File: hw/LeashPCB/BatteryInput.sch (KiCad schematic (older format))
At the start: 14 parts, among them J201 1020-1, J202 1076-1, J203 1076-1, Q201 CSD18501Q5A, Q202 Q_PMOS_DGS, U201 LM74610Q

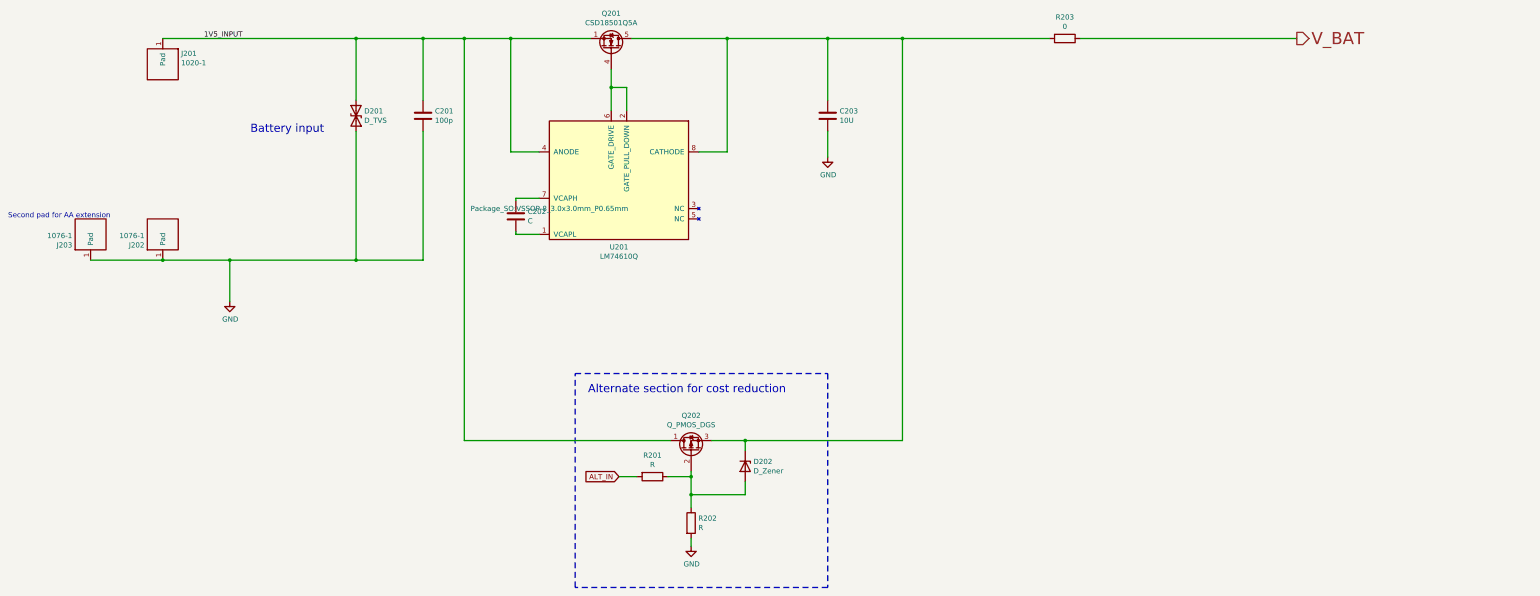
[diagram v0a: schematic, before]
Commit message: Added antenna and routed ideal diode circuit
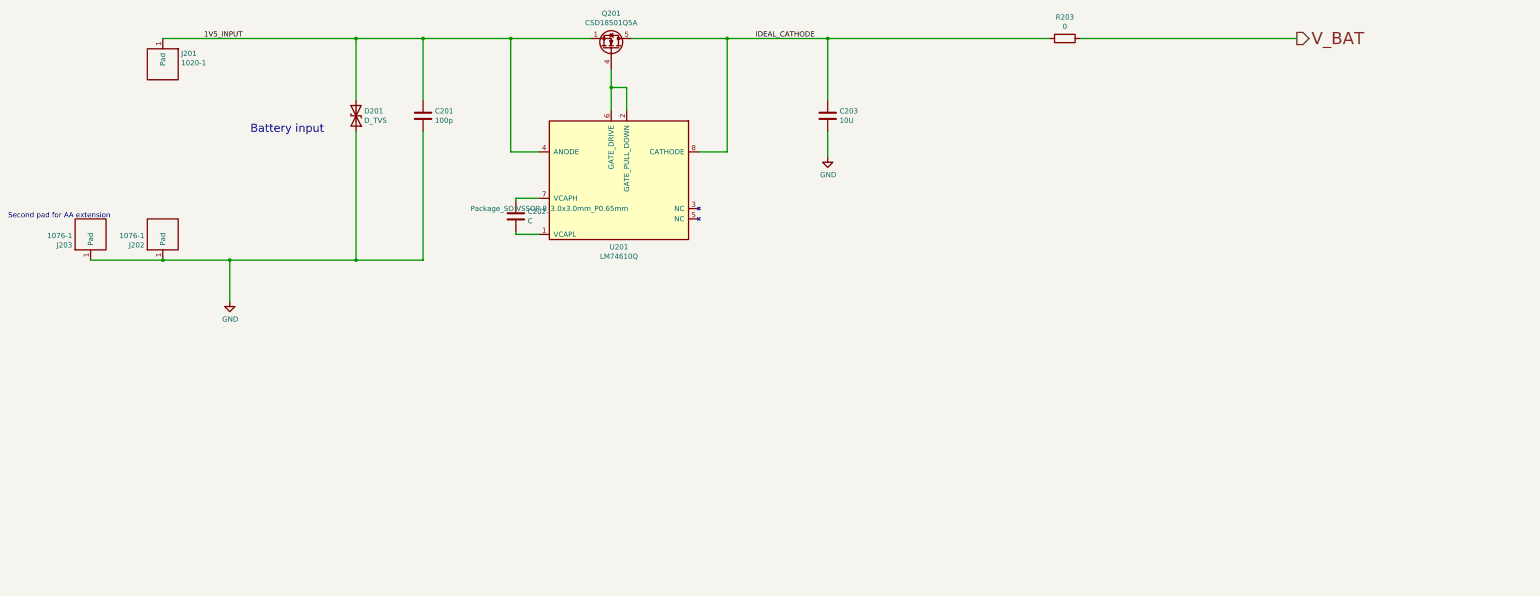
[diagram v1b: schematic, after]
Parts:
- removed D202: D_Zener, symbol Device:D_Zener
- removed Q202: Q_PMOS_DGS, symbol Device:Q_PMOS_DGS
- removed R201, R202: R, Resistor_SMD:R_0402_1005Metric, symbol Device:R
- C203: footprint Capacitor_SMD:C_0402_1005Metric -> Capacitor_SMD:C_0603_1608Metric
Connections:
- net IDEAL_CATHODE: now reaches C203.1, Q201.5 (D), R203.2, U201.8 (CATHODE)
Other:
- note removed: "Alternate section for cost reduction"
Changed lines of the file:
@@
 EESchema Schematic File Version 4
-LIBS:LeashPCB-cache
 EELAYER 29 0
 EELAYER END
@@
 F 0 "C203" H 9065 1621 50  0000 L CNN
 F 1 "10U" H 9065 1530 50  0000 L CNN
-F 2 "Capacitor_SMD:C_0402_1005Metric" H 8988 1425 50  0001 C CNN
+F 2 "Capacitor_SMD:C_0603_1608Metric" H 8988 1425 50  0001 C CNN
 F 3 "~" H 8950 1575 50  0001 C CNN
 	1    8950 1575
@@
 Connection ~ 8950 825
 Wire Wire Line
-	8950 825  9675 825
-Wire Wire Line
 	8950 1725 8950 1975
 Wire Wire Line
@@
 	5875 1925 5875 825
 Connection ~ 5875 825
-Wire Wire Line
-	5875 825  5425 825
 Text Notes 3350 1750 0    79   ~ 0
 Battery input
-Wire Wire Line
-	5425 825  5425 4725
-Connection ~ 5425 825
-Wire Wire Line
-	5425 825  5025 825
-$Comp
-L Device:Q_PMOS_DGS Q202
-U 1 1 5D1B2FC4
-P 7625 4825
-F 0 "Q202" V 7968 4825 50  0000 C CNN
-F 1 "Q_PMOS_DGS" V 7877 4825 50  0000 C CNN
-F 2 "" H 7825 4925 50  0001 C CNN
-F 3 "~" H 7625 4825 50  0001 C CNN
-	1    7625 4825
-	0    -1   -1   0
-$EndComp
-$Comp
-L Device:D_Zener D202
-U 1 1 5D1B5E6D
-P 8150 4975
-F 0 "D202" V 8104 5054 50  0000 L CNN
-F 1 "D_Zener" V 8195 5054 50  0000 L CNN
-F 2 "" H 8150 4975 50  0001 C CNN
-F 3 "~" H 8150 4975 50  0001 C CNN
-	1    8150 4975
-	0    1    1    0
-$EndComp
-$Comp
-L Device:R R202
-U 1 1 5D1B63DF
-P 7625 5525
-F 0 "R202" H 7695 5571 50  0000 L CNN
-F 1 "R" H 7695 5480 50  0000 L CNN
-F 2 "Resistor_SMD:R_0402_1005Metric" V 7555 5525 50  0001 C CNN
-F 3 "~" H 7625 5525 50  0001 C CNN
-	1    7625 5525
-	1    0    0    -1
-$EndComp
-Wire Wire Line
-	5425 4725 7425 4725
-Wire Wire Line
-	7825 4725 8150 4725
-Wire Wire Line
-	8150 4725 8150 4825
-Connection ~ 8150 4725
-Wire Wire Line
-	7625 5025 7625 5075
-Wire Wire Line
-	7625 5675 7625 5750
-Wire Wire Line
-	8150 5125 8150 5250
-Wire Wire Line
-	8150 5250 7625 5250
-Connection ~ 7625 5250
-Wire Wire Line
-	7625 5250 7625 5375
-$Comp
-L power:GND #PWR0103
-U 1 1 5D1BC7E6
-P 7625 5750
-F 0 "#PWR0103" H 7625 5500 50  0001 C CNN
-F 1 "GND" H 7630 5577 50  0000 C CNN
-F 2 "" H 7625 5750 50  0001 C CNN
-F 3 "" H 7625 5750 50  0001 C CNN
-	1    7625 5750
-	1    0    0    -1
-$EndComp
-$Comp
-L Device:R R201
-U 1 1 5D1BDEB4
-P 7250 5075
-F 0 "R201" V 7043 5075 50  0000 C CNN
-F 1 "R" V 7134 5075 50  0000 C CNN
-F 2 "Resistor_SMD:R_0402_1005Metric" V 7180 5075 50  0001 C CNN
-F 3 "~" H 7250 5075 50  0001 C CNN
-	1    7250 5075
-	0    1    1    0
-$EndComp
-Wire Wire Line
-	7400 5075 7625 5075
-Connection ~ 7625 5075
-Wire Wire Line
-	7625 5075 7625 5250
-Wire Wire Line
-	7100 5075 6925 5075
-Text GLabel 6925 5075 0    50   Input ~ 0
-ALT_IN
-Wire Wire Line
-	9675 4725 9675 825
-Wire Wire Line
-	8150 4725 9675 4725
-Connection ~ 9675 825
-Wire Notes Line
-	6500 4075 8950 4075
-Wire Notes Line
-	8950 4075 8950 6150
-Wire Notes Line
-	8950 6150 6500 6150
-Wire Notes Line
-	6500 6150 6500 4075
-Text Notes 6625 4275 0    79   ~ 0
-Alternate section for cost reduction
 $Comp
 L Device:R R203
@@
 	0    1    1    0
 $EndComp
-Wire Wire Line
-	9675 825  11100 825
 Wire Wire Line
 	11400 825  13500 825
@@
 	1800 2975 2500 2975
 Connection ~ 2500 2975
+Text Label 8250 825  0    50   ~ 0
+IDEAL_CATHODE
+Wire Wire Line
+	5025 825  5875 825
+Wire Wire Line
+	8950 825  11100 825
 $EndSCHEMATC

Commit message: Added SWD connector on the back side as a backup for testing and continued routing
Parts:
- J202, J203: footprint leash:1020-1 -> leash:1076-1
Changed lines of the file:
@@
 F 0 "J202" V 2446 2953 50  0000 L CNN
 F 1 "1076-1" V 2537 2953 50  0000 L CNN
-F 2 "leash:1020-1" H 2500 2775 50  0001 C CNN
+F 2 "leash:1076-1" H 2500 2775 50  0001 C CNN
 F 3 "" H 2500 2775 50  0001 C CNN
 F 4 "0.05" H 2500 2775 50  0001 C CNN "Standard Price"
@@
 F 0 "J203" V 1746 2953 50  0000 L CNN
 F 1 "1076-1" V 1837 2953 50  0000 L CNN
-F 2 "leash:1020-1" H 1800 2775 50  0001 C CNN
+F 2 "leash:1076-1" H 1800 2775 50  0001 C CNN
 F 3 "" H 1800 2775 50  0001 C CNN
 F 4 "0.05" H 1800 2775 50  0001 C CNN "Standard Price"

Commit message: Pulled in final small components and finished routing all but the RF section
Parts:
- D201: footprint (none) -> Diode_SMD:D_0402_1005Metric
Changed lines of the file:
@@
 F 0 "D201" V 4329 1654 50  0000 L CNN
 F 1 "D_TVS" V 4420 1654 50  0000 L CNN
-F 2 "" H 4375 1575 50  0001 C CNN
+F 2 "Diode_SMD:D_0402_1005Metric" H 4375 1575 50  0001 C CNN
 F 3 "~" H 4375 1575 50  0001 C CNN
 	1    4375 1575

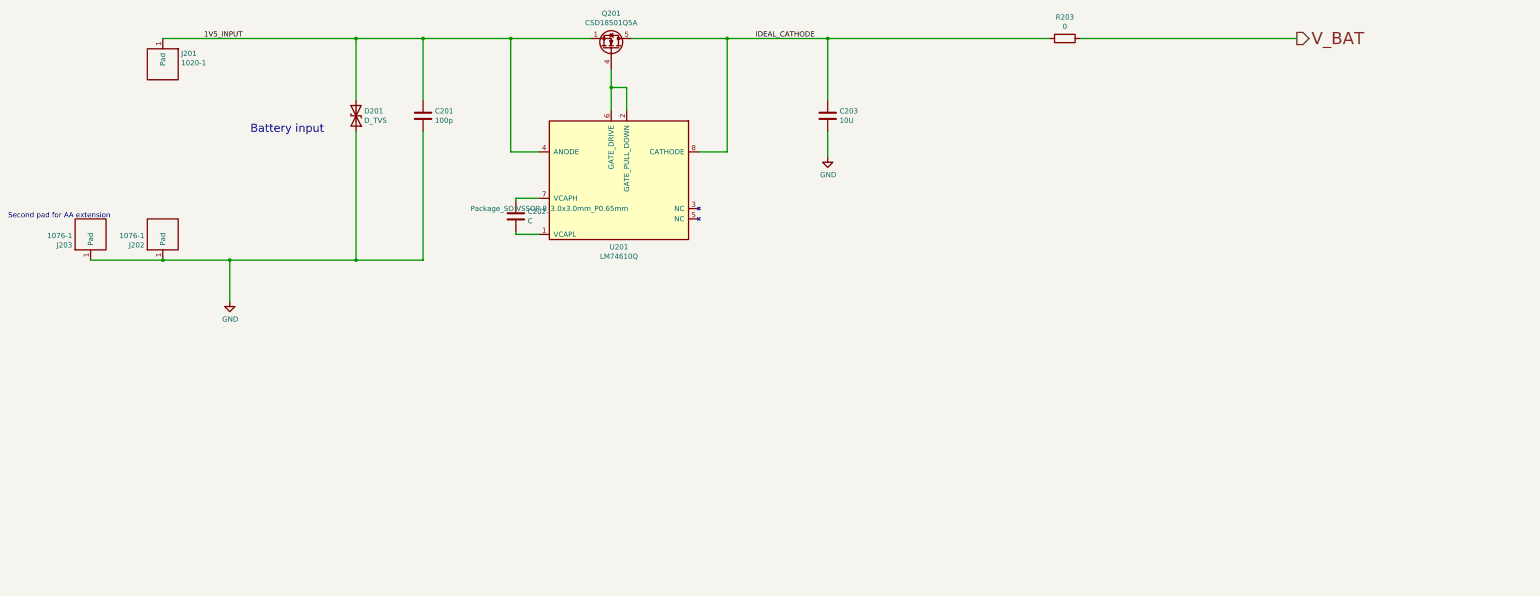
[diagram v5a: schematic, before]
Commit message: Added a switch and finished closing out DRC errors. Added a lot of via stiching in RF section.
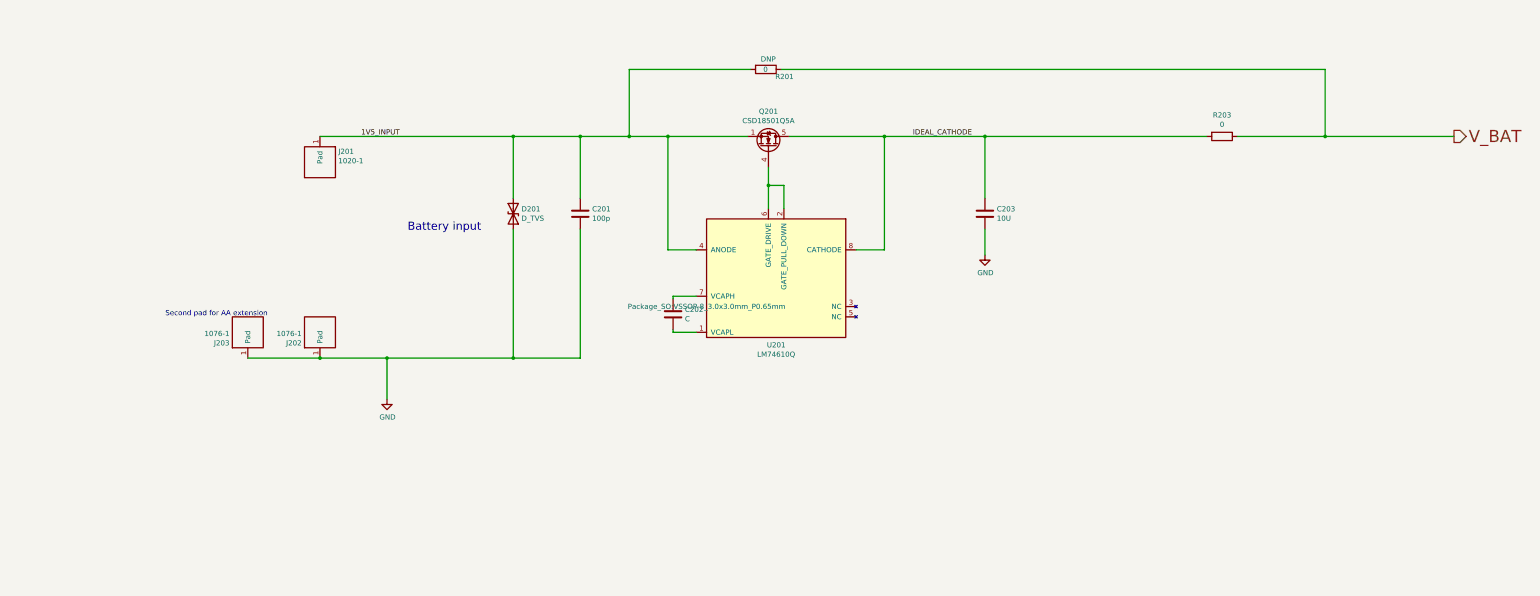
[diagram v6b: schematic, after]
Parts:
- added R201: 0, Resistor_SMD:R_0402_1005Metric, symbol Device:R
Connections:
- net 1V5_INPUT: now also R201.2
- net V_BAT: now also R201.1
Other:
- moved on the sheet: C201, C202, C203, D201, J201, J202, J203, Q201, R203, U201
